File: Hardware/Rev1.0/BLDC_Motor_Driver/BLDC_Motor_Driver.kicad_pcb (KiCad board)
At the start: 2 copper layers, 62 parts, among them Q1 IPD90N06S4L03ATMA2, Q2 IPD90N06S4L03ATMA2, Q3 IPD90N06S4L03ATMA2, Q4 IPD90N06S4L03ATMA2, Q5 IPD90N06S4L03ATMA2, Q6 IPD90N06S4L03ATMA2, U1 STM32F446RETx, U2 SPB09B-03, U3 TLV1704AQPWRQ1

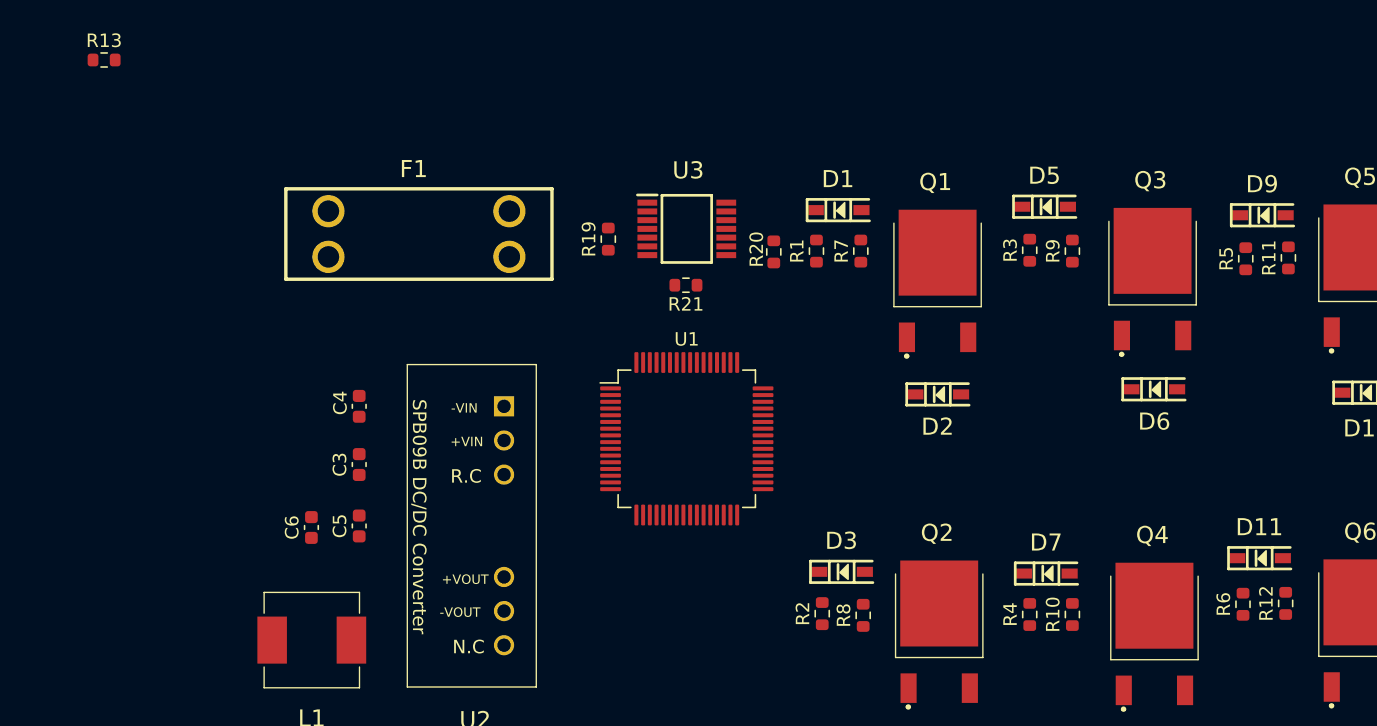
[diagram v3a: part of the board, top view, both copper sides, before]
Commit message: Started some PCB edits
Minor PCB layout edits
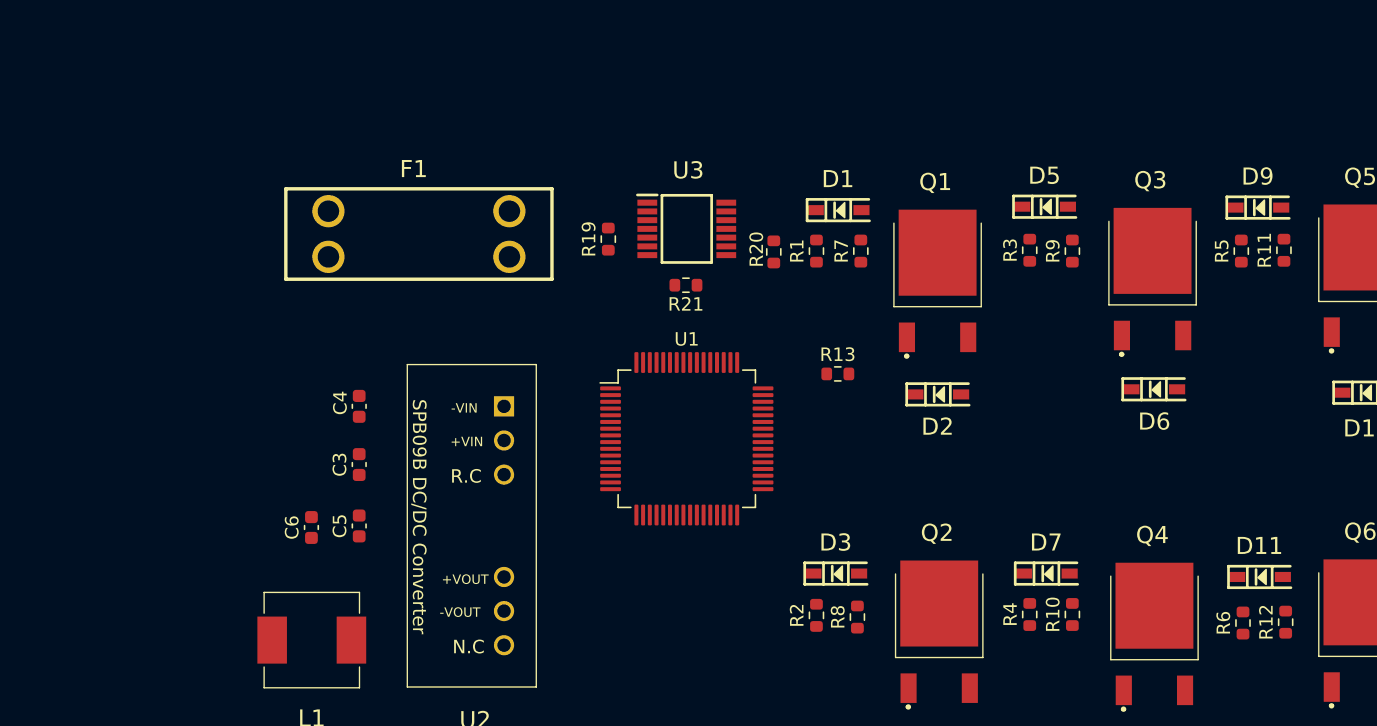
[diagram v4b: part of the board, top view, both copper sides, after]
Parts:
- moved R13 59.4 mm to (156.7, 88.3)
- moved D11 1.40 mm to (188.1, 103.4)
- moved R6 1.40 mm to (186.8, 106.8)
- moved R12 1.40 mm to (190.0, 106.7)
- moved D9 0.66 mm to (188.0, 75.9)
- moved R11 0.66 mm to (189.9, 79.1)
- moved R5 0.66 mm to (186.7, 79.1)
- moved D3 0.45 mm to (156.5, 103.1)
- moved R2 0.45 mm to (155.1, 106.2)
- moved R8 0.45 mm to (158.1, 106.4)
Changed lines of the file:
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@@
   )
   (footprint "Resistor_SMD:R_0603_1608Metric" (layer "F.Cu")
-    (at 189.992 105.346 90)
+    (at 189.992 106.743 90)
     (descr "Resistor SMD 0603 (1608 Metric), square (rectangular) end terminal, IPC_7351 nominal, (Body size source: IPC-SM-782 page 72, https://www.pcb-3d.com/wordpress/wp-content/uploads/ipc-sm-782a_amendment_1_and_2.pdf), generated with kicad-footprint-generator")
     (tags "resistor")
@@
   )
   (footprint "Diode_SMD:SOD3716X145N" (layer "F.Cu")
-    (at 188.292 76.454)
+    (at 187.96 75.883)
     (descr "SOD-123-")
     (tags "Schottky Diode")
@@
   )
   (footprint "Resistor_SMD:R_0603_1608Metric" (layer "F.Cu")
-    (at 155.497 106.108 90)
+    (at 155.067 106.235 90)
     (descr "Resistor SMD 0603 (1608 Metric), square (rectangular) end terminal, IPC_7351 nominal, (Body size source: IPC-SM-782 page 72, https://www.pcb-3d.com/wordpress/wp-content/uploads/ipc-sm-782a_amendment_1_and_2.pdf), generated with kicad-footprint-generator")
     (tags "resistor")
@@
   )
   (footprint "Diode_SMD:SOD3716X145N" (layer "F.Cu")
-    (at 188.087 101.981)
+    (at 188.087 103.378)
     (descr "SOD-123-")
     (tags "Schottky Diode")
@@
   )
   (footprint "Diode_SMD:SOD3716X145N" (layer "F.Cu")
-    (at 156.972 102.997)
+    (at 156.542 103.124)
     (descr "SOD-123-")
     (tags "Schottky Diode")
@@
   )
   (footprint "Resistor_SMD:R_0603_1608Metric" (layer "F.Cu")
-    (at 187.022 79.692 90)
+    (at 186.69 79.121 90)
     (descr "Resistor SMD 0603 (1608 Metric), square (rectangular) end terminal, IPC_7351 nominal, (Body size source: IPC-SM-782 page 72, https://www.pcb-3d.com/wordpress/wp-content/uploads/ipc-sm-782a_amendment_1_and_2.pdf), generated with kicad-footprint-generator")
     (tags "resistor")
@@
   )
   (footprint "Resistor_SMD:R_0603_1608Metric" (layer "F.Cu")
-    (at 190.197 79.629 90)
+    (at 189.865 79.058 90)
     (descr "Resistor SMD 0603 (1608 Metric), square (rectangular) end terminal, IPC_7351 nominal, (Body size source: IPC-SM-782 page 72, https://www.pcb-3d.com/wordpress/wp-content/uploads/ipc-sm-782a_amendment_1_and_2.pdf), generated with kicad-footprint-generator")
     (tags "resistor")
@@
   )
   (footprint "Resistor_SMD:R_0603_1608Metric" (layer "F.Cu")
-    (at 158.545 106.235 90)
+    (at 158.115 106.362 90)
     (descr "Resistor SMD 0603 (1608 Metric), square (rectangular) end terminal, IPC_7351 nominal, (Body size source: IPC-SM-782 page 72, https://www.pcb-3d.com/wordpress/wp-content/uploads/ipc-sm-782a_amendment_1_and_2.pdf), generated with kicad-footprint-generator")
     (tags "resistor")
@@
   )
   (footprint "Resistor_SMD:R_0603_1608Metric" (layer "F.Cu")
-    (at 102.045 64.897)
+    (at 156.655 88.265)
     (descr "Resistor SMD 0603 (1608 Metric), square (rectangular) end terminal, IPC_7351 nominal, (Body size source: IPC-SM-782 page 72, https://www.pcb-3d.com/wordpress/wp-content/uploads/ipc-sm-782a_amendment_1_and_2.pdf), generated with kicad-footprint-generator")
     (tags "resistor")
@@
   )
   (footprint "Resistor_SMD:R_0603_1608Metric" (layer "F.Cu")
-    (at 186.817 105.41 90)
+    (at 186.817 106.807 90)
     (descr "Resistor SMD 0603 (1608 Metric), square (rectangular) end terminal, IPC_7351 nominal, (Body size source: IPC-SM-782 page 72, https://www.pcb-3d.com/wordpress/wp-content/uploads/ipc-sm-782a_amendment_1_and_2.pdf), generated with kicad-footprint-generator")
     (tags "resistor")
